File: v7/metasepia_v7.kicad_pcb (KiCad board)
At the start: 2 copper layers, 237.4 x 120.8 mm, 74 parts

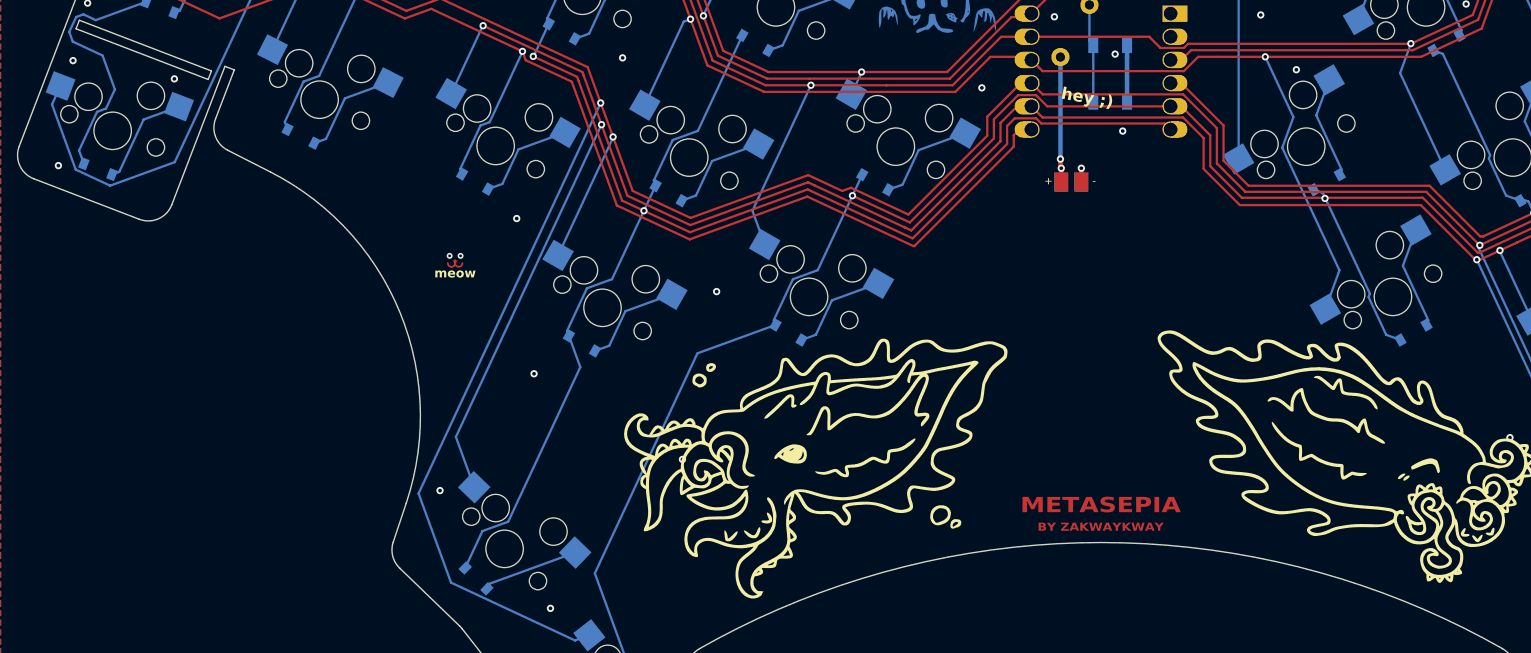
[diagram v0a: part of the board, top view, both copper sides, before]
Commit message: Send to manu
Finish metasepia7 and send to manufacture.

Modified BatteryPadsReversible footprint to use rectangular SMD pads and adjusted silk text positions. Updated metasepia_v7.kicad_pcb with a defined stackup, new net, and minor polygon coordinate corrections. Production files reorganized and backup ZIPs removed.
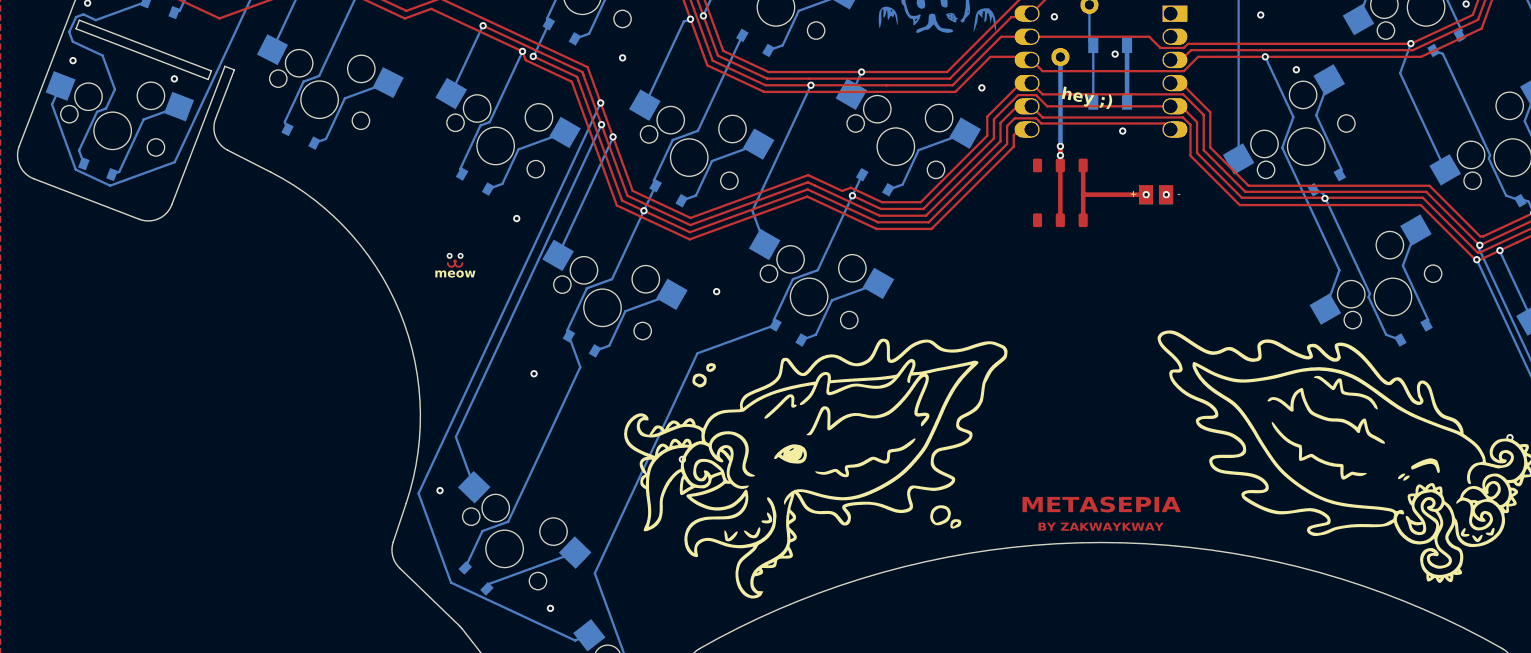
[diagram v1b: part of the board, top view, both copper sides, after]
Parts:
- added REF**: slider, frequent:slider, F.Cu at (215.1, 138.3)
- moved BT1 9.40 mm to (225.6, 138.5)
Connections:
- BT1 pad 1: BAT_POS -> battery
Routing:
- net battery: track 0.00 -> 13.5 mm, vias 0 -> 1
- net BAT_POS: track 13.1 -> 19.2 mm
- net P6: track 223.6 -> 222.4 mm
- net P7: track 183.3 -> 182.2 mm
- net P5: track 312.0 -> 311.0 mm
- net P8: track 204.3 -> 203.4 mm
- net P4: track 329.9 -> 329.0 mm
- net GND: vias 34 -> 33
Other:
- rule pad_to_mask_clearance: 0.05 -> 0.038
- board text added: "off>"

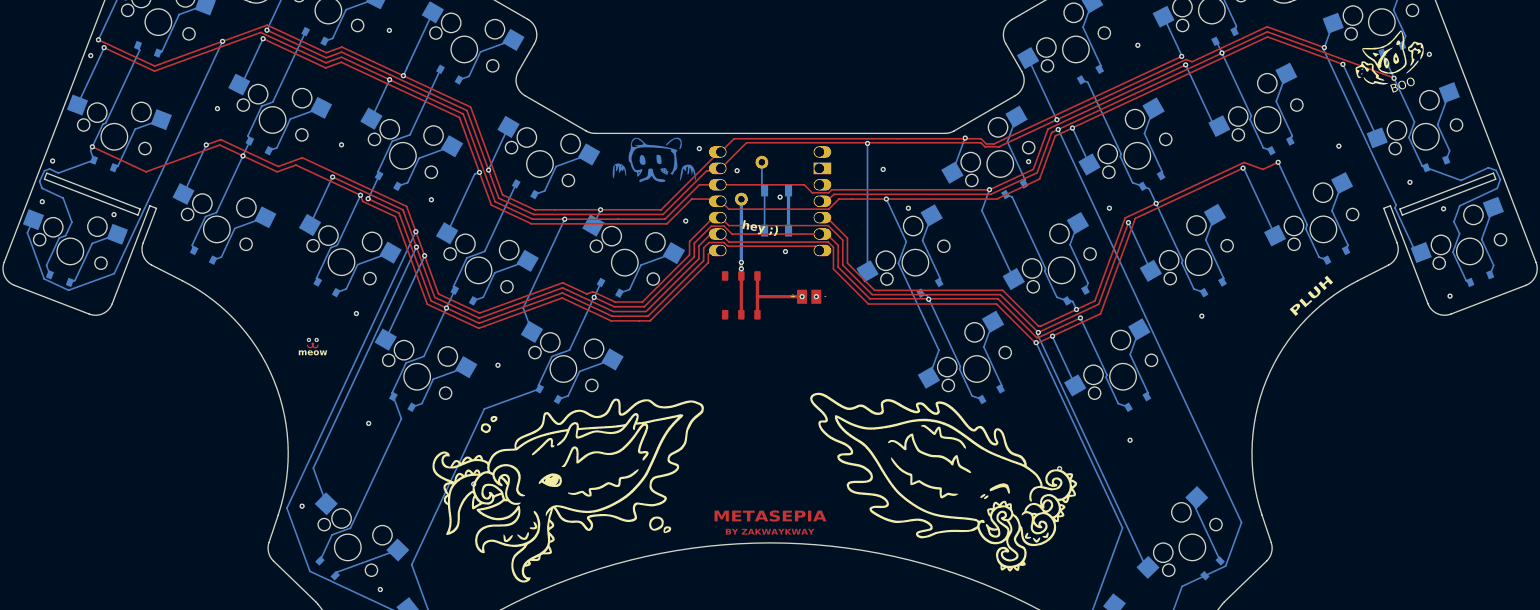
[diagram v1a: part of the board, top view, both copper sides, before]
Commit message: make breakoff tabs 2mm (were 1mm)
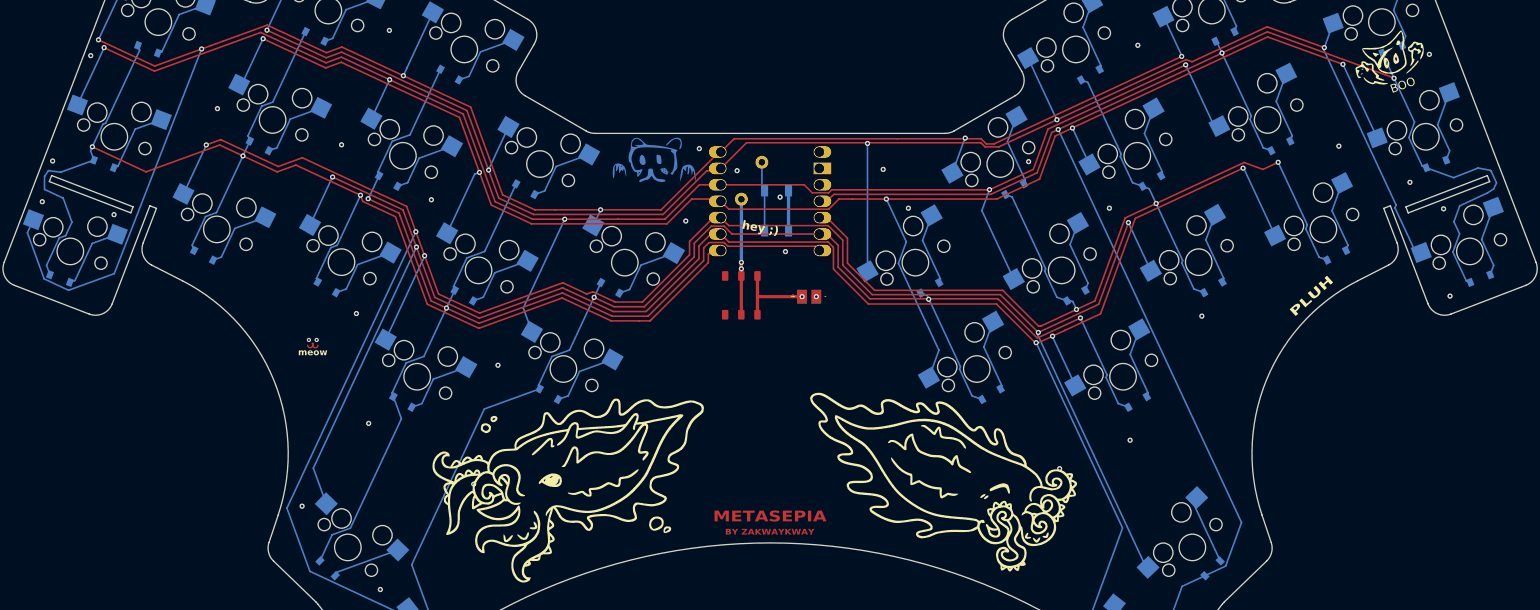
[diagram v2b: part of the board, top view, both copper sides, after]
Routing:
- net P0: track 286.4 -> 284.1 mm
- net P10: track 271.9 -> 270.5 mm
- net P6: track 222.4 -> 221.3 mm
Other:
- outline, holes or cut-outs redrawn
